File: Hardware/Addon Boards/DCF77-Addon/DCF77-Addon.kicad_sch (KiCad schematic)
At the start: 0 parts

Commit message: Version bump 2.2.0 -> new regulator and id system
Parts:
- added C1: 100u 16V, Capacitor_SMD:CP_Elec_6.3x7.7, symbol Device:C_Polarized_Small
- added D1: LED_grn, LED_SMD:LED_0805_2012Metric_Pad1.15x1.40mm_HandSolder, symbol Device:LED_Small
- added H1: GND, TestPoint:TestPoint_Loop_D3.80mm_Drill2.0mm, symbol Mechanical:MountingHole_Pad
- added J1: Misc-PortD, Connector_PinSocket_2.54mm:PinSocket_1x04_P2.54mm_Vertical, symbol Connector:Conn_01x04_Socket
- added J2: Addon_Conn, Connector_PinHeader_2.54mm:PinHeader_1x01_P2.54mm_Vertical, symbol Connector:Conn_01x01_Pin
- added J4: Misc-PortA, Connector_PinSocket_2.54mm:PinSocket_1x08_P2.54mm_Vertical, symbol Connector:Conn_01x08_Socket
- added J5: I2C, Connector_PinSocket_2.54mm:PinSocket_1x04_P2.54mm_Vertical, symbol Connector:Conn_01x04_Socket
- added J6: ST-Link, Connector_PinSocket_2.54mm:PinSocket_1x04_P2.54mm_Vertical, symbol Connector:Conn_01x04_Socket
- added J8: VDD, Connector_PinSocket_2.54mm:PinSocket_1x02_P2.54mm_Vertical, symbol Connector:Conn_01x02_Socket
- added R1, R2: 4k7, Resistor_SMD:R_0805_2012Metric_Pad1.20x1.40mm_HandSolder, symbol Device:R_Small
- added U1: AM2302, Sensor:ASAIR_AM2302_P2.54mm_Vertical, symbol Sensor:AM2302
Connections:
- new net: D1.1 (K), R2.1
- new net +3V3: C1.1, D1.2 (A), J4.1 (Pin_1), J5.1 (Pin_1), J6.4 (Pin_4), R1.1, U1.1 (VDD)
- new net A1: J4.4 (Pin_4), R1.2, U1.2 (SDA)
- new net A2: J4.6 (Pin_6)
- new net A3: J4.7 (Pin_7)
- new net A4: J4.8 (Pin_8)
- new net D0: J1.1 (Pin_1)
- new net D1: J1.2 (Pin_2)
- new net GND: C1.2, H1.1, J1.3 (Pin_3), J1.4 (Pin_4), J2.1 (Pin_1), J4.2 (Pin_2), J5.4 (Pin_4), J6.3 (Pin_3), J8.2 (Pin_2), R2.2, U1.3 (GND), U1.4 (GND)
- new net PF0: J4.3 (Pin_3)
- new net PF1: J4.5 (Pin_5)
- new net SCL: J5.2 (Pin_2)
- new net SDA: J5.3 (Pin_3)
- new net SWCLK: J6.1 (Pin_1)
- new net SWDIO: J6.2 (Pin_2)
- new net VDD: J8.1 (Pin_1)
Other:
- company: (none) -> C-Audio
- title: (none) -> DCF77 Addon Board for Nixie clock

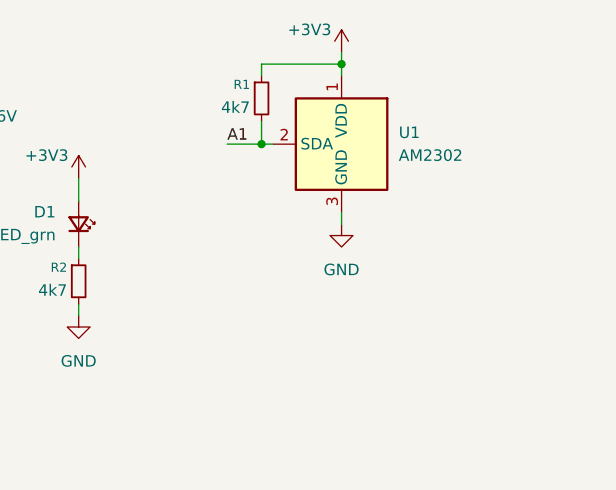
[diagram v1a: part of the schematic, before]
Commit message: finalized DCF77 board and updated 3D pictures
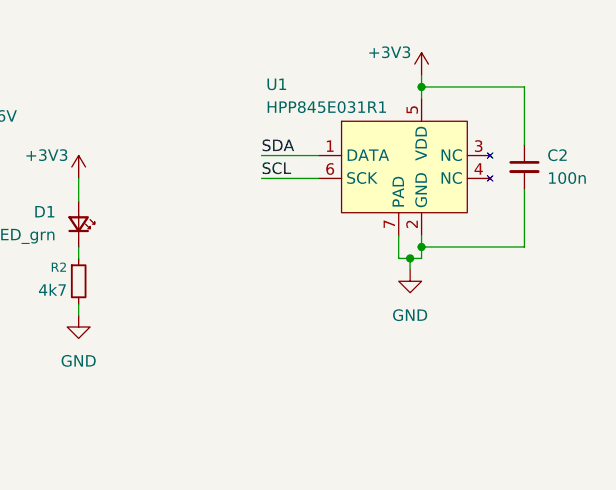
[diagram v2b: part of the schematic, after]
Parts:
- removed R1: 4k7, Resistor_SMD:R_0805_2012Metric_Pad1.20x1.40mm_HandSolder, symbol Device:R_Small
- removed U1: AM2302, Sensor:ASAIR_AM2302_P2.54mm_Vertical, symbol Sensor:AM2302
- added C2: 100n, Capacitor_SMD:C_0805_2012Metric_Pad1.18x1.45mm_HandSolder, symbol Device:C_Small
- added U1: HPP845E031R1, Package_DFN_QFN:Maxim_TDFN-6-1EP_3x3mm_P0.95mm_EP1.5x2.3mm, symbol HPP845E031R1:HPP845E031R1
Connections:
- net +3V3: now also C2.1, U1.5 (VDD)
- net GND: now also C2.2, U1.2 (GND), U1.7 (PAD)
- net SCL: now also U1.6 (SCK)
- net SDA: now also U1.1 (DATA)

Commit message: finalized addon board and produced fabrication outputs
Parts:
- added C3: 100n, Capacitor_SMD:C_0805_2012Metric_Pad1.18x1.45mm_HandSolder, symbol Device:C_Small
- added D2: LED_grn, LED_SMD:LED_0805_2012Metric_Pad1.15x1.40mm_HandSolder, symbol Device:LED_Small
- added R1: 4k7, Resistor_SMD:R_0805_2012Metric_Pad1.20x1.40mm_HandSolder, symbol Device:R_Small
- added U2: DCF77-Module, DCF77-Module:DCF77-Module, symbol DCF77-Reciever:DCF77-Module
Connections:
- net +3V3: now also C3.1, D2.2 (A), U2.4 (VDD)
- net A1: now also U2.1 (En)
- net A2: now also U2.2 (DATA)
- net GND: now also C3.2, R1.2, U2.3 (GND)
- new net: D2.1 (K), R1.1
- no-connect marks 0 -> 4
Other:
- moved on the sheet: C1, C2, D1, H1, J5, J6, J8, R2, U1
